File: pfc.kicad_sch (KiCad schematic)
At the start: 30 parts, among them Q3 IRF840, U1 LM324, U3 TC4427

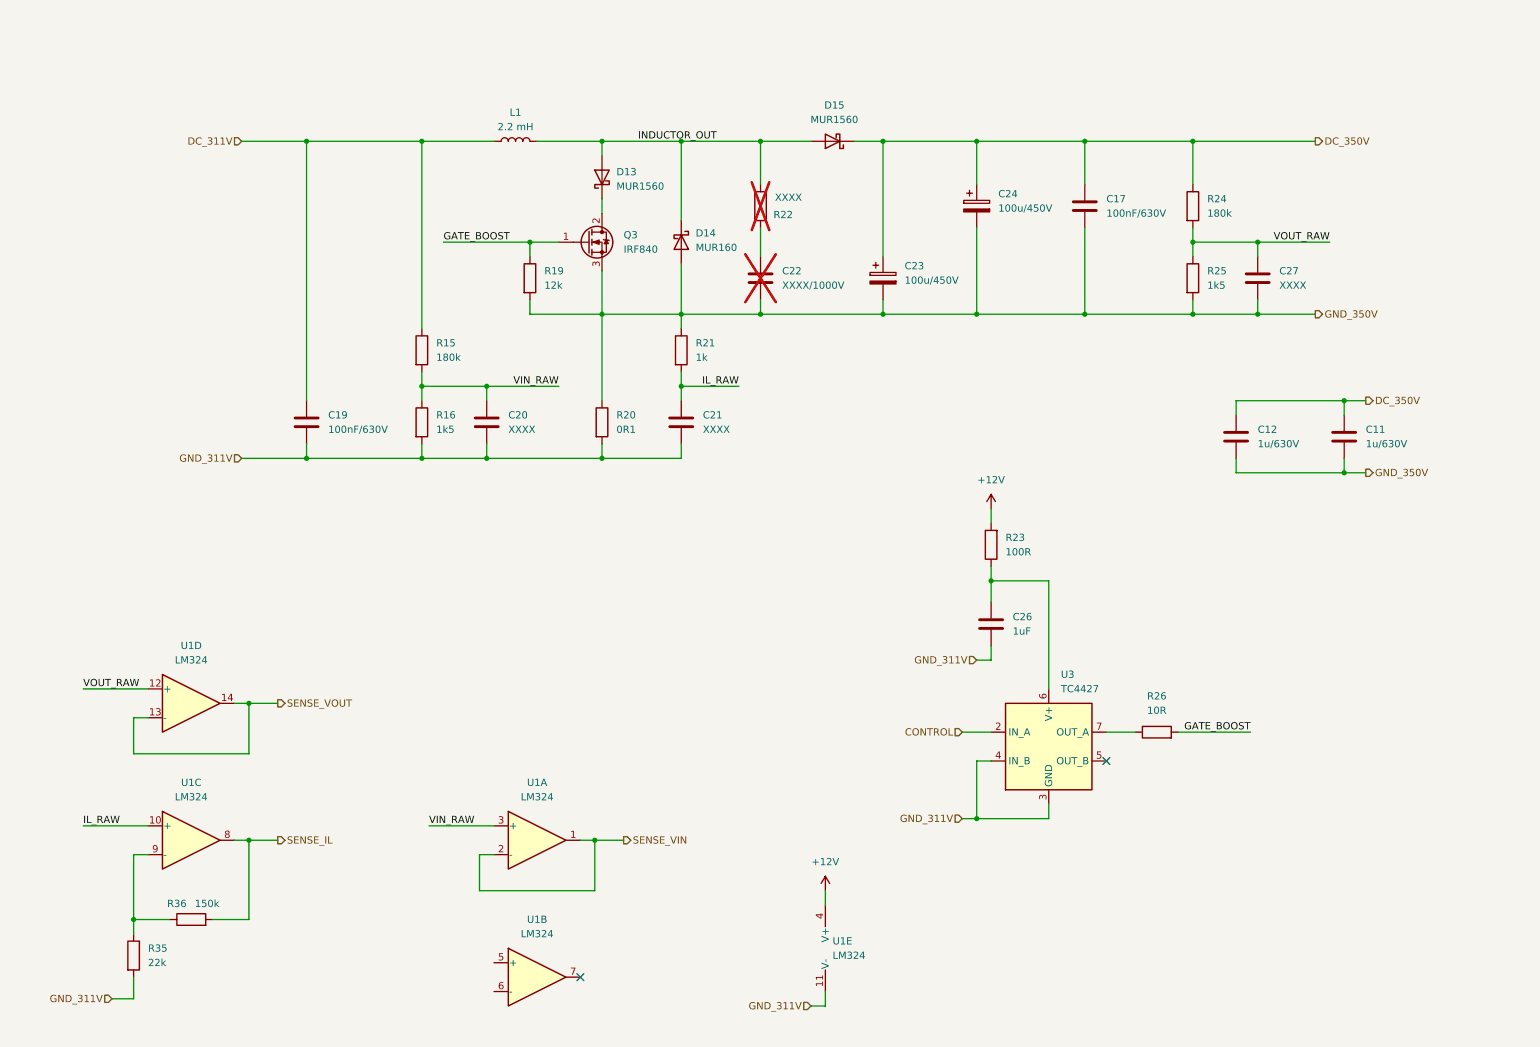
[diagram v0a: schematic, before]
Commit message: docs: add 3D renders, comprehensive README, CERN-OHL-S license, and update PCB routing
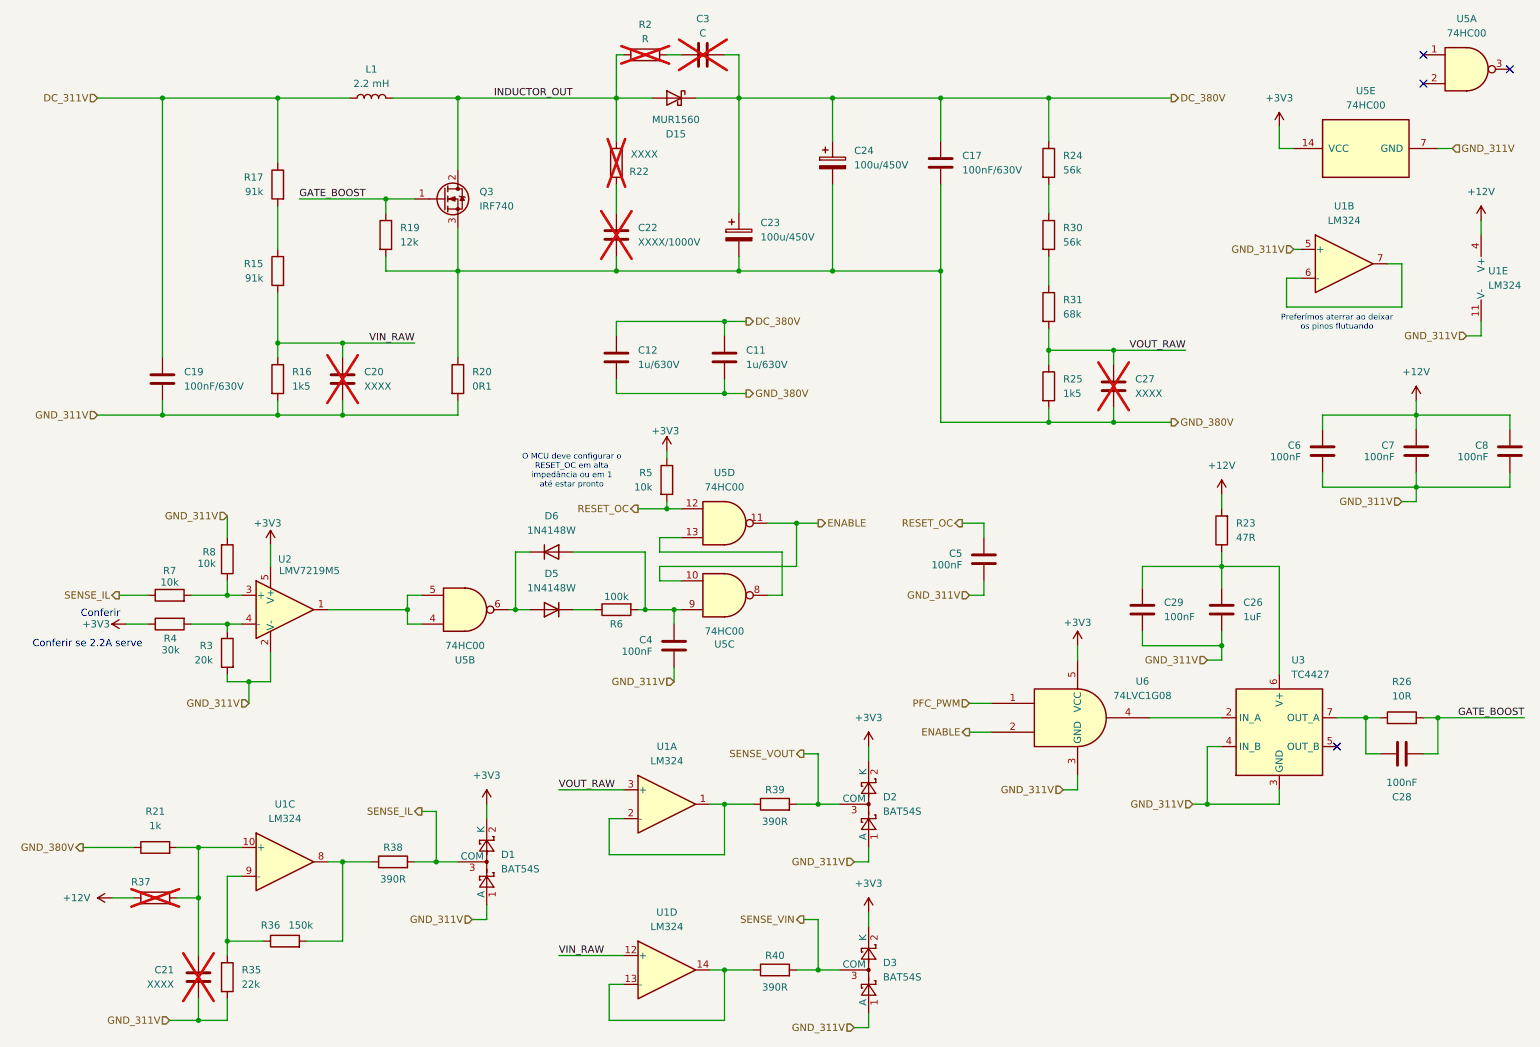
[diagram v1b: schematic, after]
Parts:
- removed D13: MUR1560, Package_TO_SOT_THT:TO-220-2_Vertical, symbol Device:D_Schottky
- removed D14: MUR160, Diode_THT:D_DO-41_SOD81_P10.16mm_Horizontal, symbol Device:D_Schottky
- added C28, C29, C4, C5, C6, C7, C8: 100nF, Capacitor_SMD:C_1206_3216Metric_Pad1.33x1.80mm_HandSolder, symbol Device:C
- added C3: C, Capacitor_SMD:C_1812_4532Metric_Pad1.57x3.40mm_HandSolder, symbol Device:C
- added D1, D2, D3: BAT54S, Package_TO_SOT_SMD:SOT-23, symbol Diode:BAT54S
- added D5, D6: 1N4148W, Diode_SMD:D_SOD-123, symbol Diode:1N4148W
- added R17: 91k, Resistor_SMD:R_1206_3216Metric_Pad1.30x1.75mm_HandSolder, symbol Device:R
- added R2: R, Resistor_SMD:R_2512_6332Metric_Pad1.40x3.35mm_HandSolder, symbol Device:R
- added R3: 20k, Resistor_SMD:R_1206_3216Metric_Pad1.30x1.75mm_HandSolder, symbol Device:R
- added R30: 56k, Resistor_SMD:R_1206_3216Metric_Pad1.30x1.75mm_HandSolder, symbol Device:R
- added R31: 68k, Resistor_SMD:R_1206_3216Metric_Pad1.30x1.75mm_HandSolder, symbol Device:R
- added R37: (no value), Resistor_SMD:R_1206_3216Metric_Pad1.30x1.75mm_HandSolder, symbol Device:R
- added R38, R39, R40: 390R, Resistor_SMD:R_1206_3216Metric_Pad1.30x1.75mm_HandSolder, symbol Device:R
- added R4: 30k, Resistor_SMD:R_1206_3216Metric_Pad1.30x1.75mm_HandSolder, symbol Device:R
- added R5, R7, R8: 10k, Resistor_SMD:R_1206_3216Metric_Pad1.30x1.75mm_HandSolder, symbol Device:R
- added R6: 100k, Resistor_SMD:R_1206_3216Metric_Pad1.30x1.75mm_HandSolder, symbol Device:R
- added U2: LMV7219M5, Package_TO_SOT_SMD:SOT-23-5, symbol Comparator:LMV7219M5
- added U5: 74HC00, Package_SO:SOIC-14_3.9x8.7mm_P1.27mm, symbol 74xx:74HC00
- added U6: 74LVC1G08, Package_TO_SOT_SMD:SOT-23-5_HandSoldering, symbol 74xGxx:74LVC1G08
- C11, C12: footprint Capacitor_THT:C_Rect_L18.0mm_W11.0mm_P15.00mm_FKS3_FKP3 -> MyCapacitors:Capacitorzao
- C20, C21, C27: now not fitted
- D15: footprint Package_TO_SOT_THT:TO-220-2_Vertical -> Package_TO_SOT_THT:TO-220-2_Horizontal_TabUp
- Q3: value IRF840 -> IRF740; footprint Package_TO_SOT_THT:TO-220-3_Vertical -> Package_TO_SOT_THT:TO-220-3_Horizontal_TabUp
- R15: value 180k -> 91k
- R23: value 100R -> 47R
- R24: value 180k -> 56k
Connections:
- net +12V: now also C6.1, C7.1, C8.1, R37.1
- net DC_311V: now also L1.2, R17.1; no longer L1.1, R15.1
- net GATE_BOOST: now also C28.2
- net GND_311V: now also U1.5 (+), C29.2, C4.2, C5.2, C6.2, C7.2, C8.2, D1.1 (A), D2.1 (A), D3.1 (A), R3.2, R8.2, U2.2 (V-), U5.7 (GND), U6.3 (GND)
- net INDUCTOR_OUT: now also L1.1, Q3.2 (D), R2.1; no longer L1.2
- net SENSE_IL: now also D1.3 (COM), R38.2, R7.1; no longer R36.2, U1.8
- net SENSE_VIN: now also D3.3 (COM), R40.2; no longer U1.1, U1.2 (-)
- net SENSE_VOUT: now also D2.3 (COM), R39.2; no longer U1.13 (-), U1.14
- net VIN_RAW: now also U1.12 (+); no longer U1.3 (+)
- net VOUT_RAW: now also U1.3 (+), R31.2; no longer R24.2, U1.12 (+)
- net at C26.1, R23.1, U3.6 (V+): now also C29.1
- net at R26.1, U3.7 (OUT_A): now also C28.1
- net at U1.6 (-): now also U1.7
- net CONTROL: no longer names the net of U3.2 (IN_A)
- net CONTROL: now also U6.4
- net DC_350V renamed DC_380V
- net DC_380V: now also C3.2
- net GND_350V renamed GND_380V
- net IL_RAW: no longer names the net of C21.1, R21.2, U1.10 (+)
- net IL_RAW: now also R37.2
- new net: U5.13, U5.8
- new net: R39.1, U1.1, U1.2 (-)
- new net: R36.2, R38.1, U1.8
- new net: R7.2, R8.1, U2.3 (+)
- new net: C3.1, R2.2
- new net: R30.2, R31.1
- new net: C4.1, D6.2 (A), R6.2, U5.9
- new net: R15.1, R17.2
- new net: D5.1 (K), R6.1
- new net: D5.2 (A), D6.1 (K), U5.6
- new net: R3.1, R4.2, U2.4 (-)
- new net: R24.2, R30.1
- new net: U2.1, U5.4, U5.5
- new net: R40.1, U1.13 (-), U1.14
- new net +3V3: D1.2 (K), D2.2 (K), D3.2 (K), R4.1, R5.1, U2.5 (V+), U5.14 (VCC), U6.5 (VCC)
- new net ENABLE: U5.10, U5.11, U6.2
- new net PFC_PWM: U6.1
- new net RESET_OC: C5.1, R5.2, U5.12
- no-connect marks 2 -> 4
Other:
- note added: "Conferir"
- note added: "Conferir se 2.2A serve"
- note added: "O MCU deve configurar o RESET_OC em alta impedância ou em 1 até estar pronto"
- note added: "Preferímos aterrar ao deixar os pinos flutuando"
- moved on the sheet: C11, C12, C17, C19, C22, C23, C24, C26, D15, Q3, R15, R16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

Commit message: pcb: atualizar layout 2D da placa e esquematicos
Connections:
- net ENABLE: now also U5.3, U5.5; no longer U5.10, U5.11
- net RESET_OC: now also U5.1; no longer U5.12
- net at U5.8: now also D5.2 (A), D6.1 (K); no longer U5.13
- net at C4.1, D6.2 (A), R6.2: now also U5.4; no longer U5.9
- net at U5.2: now also U5.6
- new net: U2.1, U5.10, U5.9
